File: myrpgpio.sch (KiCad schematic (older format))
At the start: 31 parts, among them U1 8xLEVEL_SHIFT, U2 24LC512, U3 24LC512, U4 MCP3304, U5 OPT101

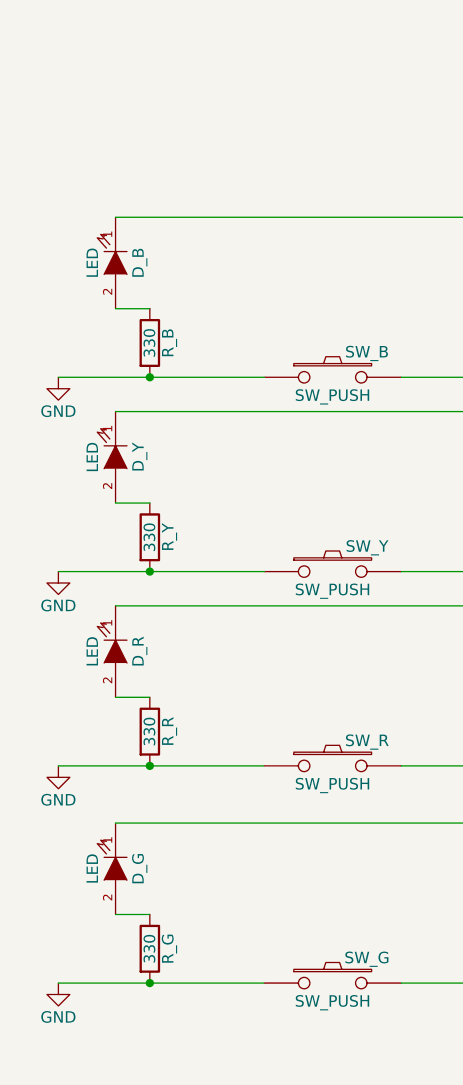
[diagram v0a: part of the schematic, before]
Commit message: Fix power connections on LEDs (wired active-low)
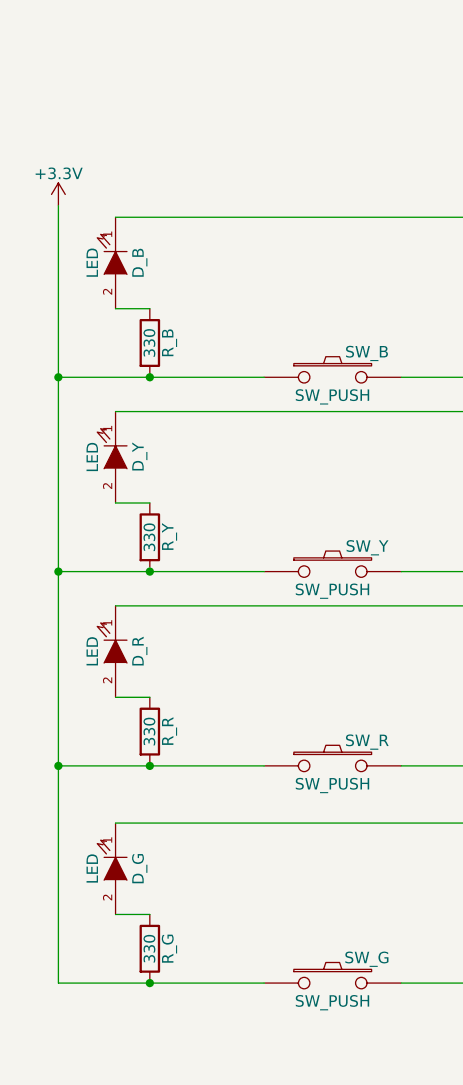
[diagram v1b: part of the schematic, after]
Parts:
- gave numbers to parts that had none: 9
- renumbered D1 to Dz
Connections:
- net +3V3: now also R_B.2, R_G.2, R_R.2, R_Y.2, SW_B.1, SW_G.1, SW_R.1, SW_Y.1
- net GND: no longer R_B.2, R_G.2, R_R.2, R_Y.2, SW_B.1, SW_G.1, SW_R.1, SW_Y.1
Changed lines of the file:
@@
 LIBS:contrib
 LIBS:valves
-LIBS:0mymisc
 LIBS:myrpgpio-cache
 EELAYER 25 0
@@
 $EndComp
 $Comp
-L GND #PWR?
-U 1 1 58060081
-P 800 8550
-F 0 "#PWR?" H 800 8300 50  0001 C CNN
-F 1 "GND" H 800 8400 50  0000 C CNN
-F 2 "" H 800 8550 50  0000 C CNN
-F 3 "" H 800 8550 50  0000 C CNN
-	1    800  8550
-	1    0    0    -1
-$EndComp
-$Comp
-L GND #PWR?
-U 1 1 580600CE
-P 800 9500
-F 0 "#PWR?" H 800 9250 50  0001 C CNN
-F 1 "GND" H 800 9350 50  0000 C CNN
-F 2 "" H 800 9500 50  0000 C CNN
-F 3 "" H 800 9500 50  0000 C CNN
-	1    800  9500
-	1    0    0    -1
-$EndComp
-$Comp
-L GND #PWR?
-U 1 1 5806011B
-P 800 7700
-F 0 "#PWR?" H 800 7450 50  0001 C CNN
-F 1 "GND" H 800 7550 50  0000 C CNN
-F 2 "" H 800 7700 50  0000 C CNN
-F 3 "" H 800 7700 50  0000 C CNN
-	1    800  7700
-	1    0    0    -1
-$EndComp
-$Comp
-L GND #PWR?
-U 1 1 58060168
-P 800 6850
-F 0 "#PWR?" H 800 6600 50  0001 C CNN
-F 1 "GND" H 800 6700 50  0000 C CNN
-F 2 "" H 800 6850 50  0000 C CNN
-F 3 "" H 800 6850 50  0000 C CNN
-	1    800  6850
-	1    0    0    -1
-$EndComp
-$Comp
-L Q_NPN_EBC Q?
+L Q_NPN_EBC Qz
 U 1 1 580621C0
 P 13200 2100
@@
 $EndComp
 $Comp
-L R R?
+L R Rz
 U 1 1 58062225
 P 12850 2100
@@
 $EndComp
 $Comp
-L D D1
+L D Dz
 U 1 1 580622C7
 P 13300 1600
@@
 $EndComp
 $Comp
-L INDUCTOR L?
+L INDUCTOR Lz
 U 1 1 580626E5
 P 14200 1600
@@
 yellow
 $Comp
-L R R?
+L R Rf
 U 1 1 58064A73
 P 11250 3100
@@
 $EndComp
 $Comp
-L Q_NPN_CBE Q?
+L Q_NPN_CBE Qf
 U 1 1 58064C64
 P 11600 3100
@@
 $EndComp
 $Comp
-L D D?
+L D Df
 U 1 1 58064EB1
 P 11700 2650
@@
 $EndComp
 $Comp
-L INDUCTOR L?
+L INDUCTOR Lf
 U 1 1 58065BB0
 P 12900 2900
@@
 $EndComp
 $Comp
-L INDUCTOR L?
+L INDUCTOR Lt
 U 1 1 580693A8
 P 13750 5300
@@
 $EndComp
 $Comp
-L MW8675W_7SEG 4x7SEG?
+L MW8675W_7SEG 4x7SEG1
 U 1 1 5805E479
 P 1400 2800
@@
 Wire Wire Line
 	3800 2900 8650 2900
+$Comp
+L +3.3V #PWR?
+U 1 1 5805CFB3
+P 800 6100
+F 0 "#PWR?" H 800 5950 50  0001 C CNN
+F 1 "+3.3V" H 800 6240 50  0000 C CNN
+F 2 "" H 800 6100 50  0000 C CNN
+F 3 "" H 800 6100 50  0000 C CNN
+	1    800  6100
+	1    0    0    -1
+$EndComp
+Wire Wire Line
+	800  6100 800  9500
+Connection ~ 800  6850
+Connection ~ 800  7700
+Connection ~ 800  8550
 $EndSCHEMATC
